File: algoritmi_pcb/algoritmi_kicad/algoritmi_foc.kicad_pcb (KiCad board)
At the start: 2 copper layers, 27 parts, among them IC1 MA710GQ-Z, IC2 AP2114HA-3.3TRG1, U1 TMC6300-LA-T

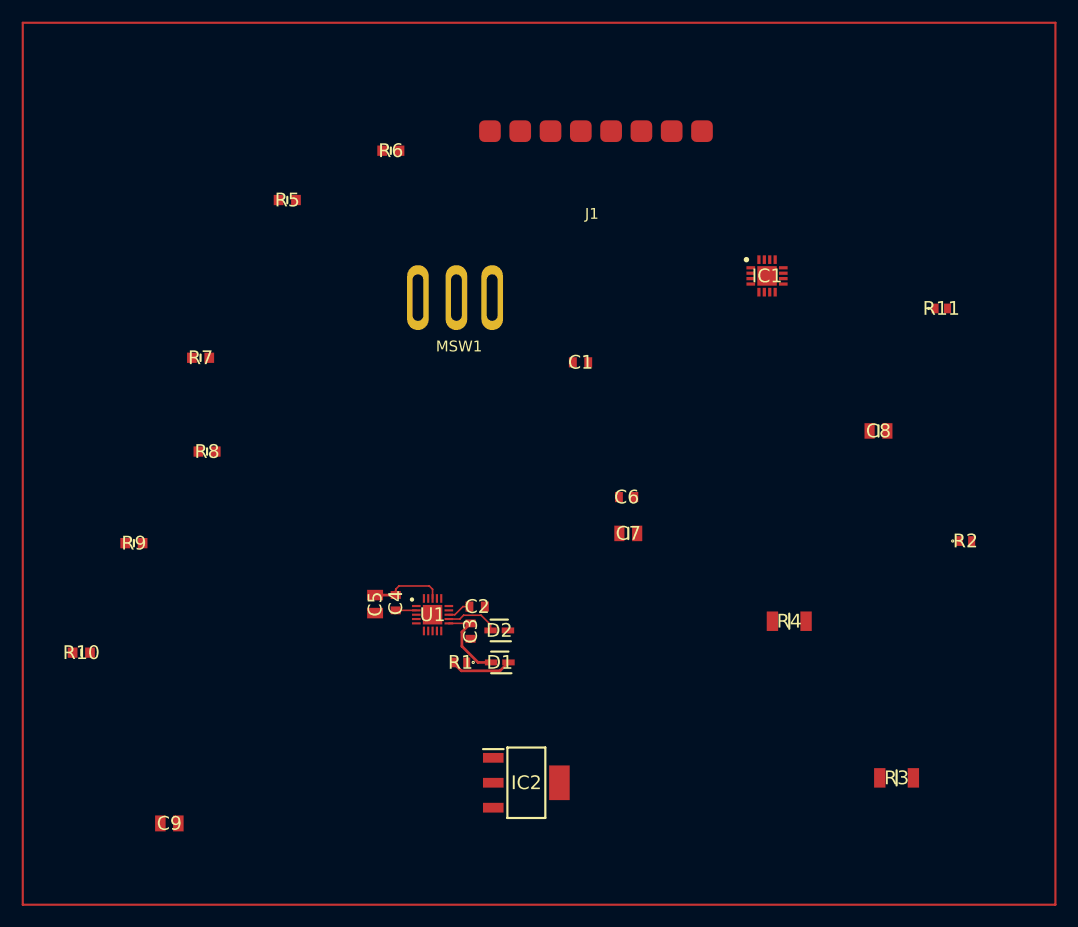
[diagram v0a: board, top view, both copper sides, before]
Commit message: Update PCB and Design
Design: added the connector for the motor.

PCB: added some constraints and essentially connected all the components to the TMC6300-LA-T.
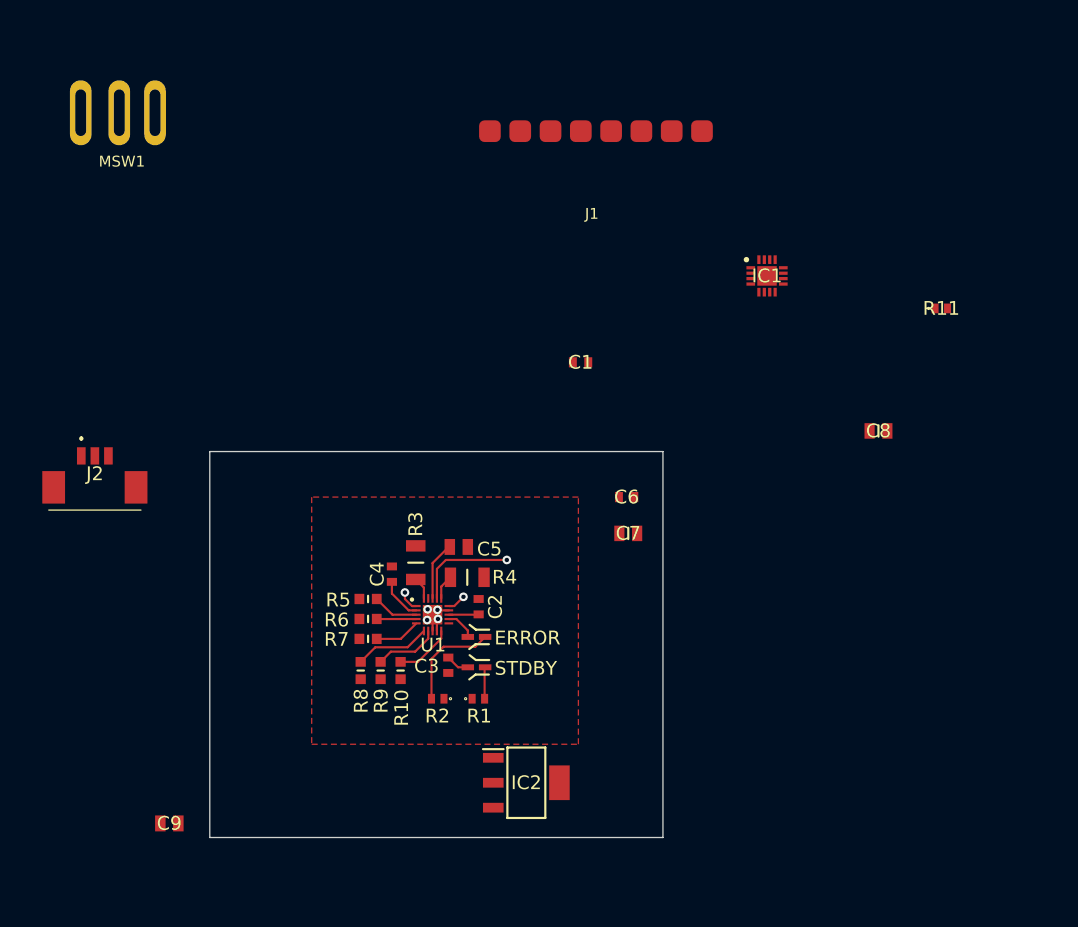
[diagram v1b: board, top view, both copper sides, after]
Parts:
- added J2: 53261-0371, SamacSys_Parts:532610371, F.Cu at (91.6, 106.3)
- moved R2 50.8 mm to (123.2, 125.8), turned to 180 degrees
- moved R3 48.6 mm to (121.2, 113.2), turned to 90 degrees
- moved R6 43.2 mm to (116.8, 118.4)
- moved R5 37.5 mm to (116.8, 116.6)
- moved MSW1 35.5 mm to (94.1, 76.8)
- moved R7 30.2 mm to (116.8, 120.3)
- moved R4 30.0 mm to (126.0, 114.6)
- moved R10 29.5 mm to (119.8, 123.2), turned to 90 degrees
- moved R9 25.6 mm to (118.0, 123.2), turned to 90 degrees
- moved R8 24.7 mm to (116.1, 123.2), turned to 90 degrees
- moved C5 9.35 mm to (125.2, 111.8), turned to 180 degrees
- moved C3 3.76 mm to (124.2, 122.7)
- moved R1 3.73 mm to (127.0, 125.8), turned to 0 degrees
- moved C4 2.65 mm to (119.0, 114.3)
- moved D1 2.20 mm to (126.8, 122.9)
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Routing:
- net V_OUT: track 0.00 -> 9.52 mm, vias 0 -> 1
- net Net-(D2-K): track 0.00 -> 9.47 mm
- net UL: track 0.00 -> 7.01 mm
- net GND: track 0.00 -> 6.24 mm, vias 0 -> 4
- net WL: track 0.00 -> 5.98 mm
- net Net-(D1-A): track 7.78 -> 2.17 mm
- net VL: track 0.00 -> 5.34 mm
- net UH: track 0.00 -> 4.25 mm
- net WH: track 0.00 -> 4.24 mm
- net VH: track 0.00 -> 3.65 mm
- net Net-(D1-K): track 5.72 -> 2.92 mm
- net BRUV: track 0.00 -> 2.30 mm
- net Net-(D2-A): track 4.88 -> 2.78 mm
- net VCP: track 1.90 -> 3.97 mm
- net BRW: track 0.00 -> 2.06 mm
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- added copper zone on F.Cu, net GND
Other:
- board outline added: 41.8 x 35.6 mm

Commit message: More PCB and Schematics Design
Also added components to the library.
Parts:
- added J3: SMM-115-02-S-D-LC-K-TR, SamacSys_Parts:SMM11502SDLCKTR, F.Cu at (179.0, 85.1)
- added MSW2: ~, solder_pads:solder_pads_4mm_3, F.Cu at (66.6, 133.5)
- added MSW3: ~, solder_pads:solder_pads_4mm_3, F.Cu at (66.6, 142.8)
- added MSW4: ~, solder_pads:solder_pads_4mm_3, F.Cu at (66.6, 152.0)
- added R12: 300R, SamacSys_Parts:ERJUP3, F.Cu at (73.5, 126.9)
- added R13: 300R, SamacSys_Parts:ERJUP3, F.Cu at (73.5, 130.8)
- added R14: 300R, SamacSys_Parts:ERJUP3, F.Cu at (73.5, 134.6)
- IC1: moved to B.Cu
- moved C5 144.3 mm to (269.4, 118.1)
- moved C3 144.3 mm to (268.4, 129.3)
- moved R3 144.3 mm to (265.4, 119.8)
- moved R4 144.3 mm to (270.1, 121.2)
- moved R9 144.3 mm to (262.1, 129.8)
- moved R1 144.3 mm to (271.1, 132.4)
- moved R2 144.3 mm to (267.4, 132.4)
- moved C2 144.3 mm to (271.1, 123.9)
- moved C4 144.3 mm to (263.1, 120.9)
- moved D1 144.3 mm to (270.9, 129.5)
- moved D2 144.3 mm to (270.9, 126.7)
- moved R10 144.3 mm to (263.9, 129.8)
- moved R5 144.3 mm to (260.9, 123.2)
- moved R6 144.3 mm to (260.9, 125.0)
- moved R7 144.3 mm to (260.9, 126.8)
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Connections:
- R11 pad 1: SW_OUT -> SW1_OUT
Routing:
- net VS: track 5.47 -> 20.2 mm
- net Net-(D2-K): track 9.47 -> 14.2 mm
- net Net-(D1-A): track 2.17 -> 5.80 mm
- net U_OUT: track 1.70 -> 4.00 mm, vias 1 -> 2
- net W_OUT: track 1.92 -> 4.13 mm, vias 1 -> 2
- net V_OUT: track 9.52 -> 10.1 mm, vias 1 -> 2
- removed copper zone on F.Cu, net GND

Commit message: PCB v0 Finished
PCB design ended, version 0
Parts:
- removed MSW1: ~, solder_pads:solder_pads_4mm_3
- removed R11: 300R, SamacSys_Parts:ERJUP3
- added H1: MotorHole, Holes:MountingHole_M1.6, F.Cu at (102.2, 66.6)
- added H2: MotorHole, Holes:MountingHole_M1.6, F.Cu at (86.9, 57.7)
- added H3: MotorHole, Holes:MountingHole_M1.6, F.Cu at (102.2, 48.8)
- added H4: MountHole, Holes:MountingHole_2.2mm_M2_ISO7380_Pad_NonVirtual, F.Cu at (97.1, 87.5)
- added H5: MountHole, Holes:MountingHole_2.2mm_M2_ISO7380_Pad_NonVirtual, F.Cu at (67.3, 57.7)
- added H6: MountHole, Holes:MountingHole_2.2mm_M2_ISO7380_Pad_NonVirtual, F.Cu at (97.1, 27.9)
- added H7: MountHole, Holes:MountingHole_2.2mm_M2_ISO7380_Pad_NonVirtual, F.Cu at (126.9, 57.7)
- C9, J1, J2: moved to B.Cu
- IC1: moved to F.Cu
- moved C3 146.5 mm to (127.1, 90.1)
- moved R3 146.5 mm to (124.1, 80.6)
- moved R9 146.5 mm to (120.9, 90.6)
- moved C5 146.5 mm to (128.2, 78.9)
- moved D1 146.5 mm to (129.7, 90.3)
- moved D2 146.5 mm to (129.7, 87.5)
- moved R1 146.5 mm to (129.9, 93.2)
- moved R10 146.5 mm to (122.7, 90.6)
- moved R2 146.5 mm to (126.2, 93.2)
- moved R5 146.5 mm to (119.7, 84.0)
- moved R6 146.5 mm to (119.7, 85.8)
- moved R7 146.5 mm to (119.7, 87.7)
- moved C2 146.5 mm to (129.9, 84.7)
- moved C4 146.5 mm to (121.9, 81.7)
- moved R8 146.5 mm to (119.1, 90.6)
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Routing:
- net VS: track 20.2 -> 256.7 mm, vias 0 -> 4
- net VL: track 5.34 -> 154.7 mm, vias 0 -> 2
- net WL: track 5.98 -> 154.2 mm, vias 0 -> 2
- net WH: track 4.24 -> 152.0 mm, vias 0 -> 2
- net UL: track 7.01 -> 151.6 mm, vias 0 -> 2
- net VH: track 3.65 -> 147.3 mm, vias 0 -> 2
- net UH: track 4.25 -> 124.3 mm, vias 0 -> 2
- net +3.3V: track 0.00 -> 101.1 mm, vias 0 -> 1
- net GND: track 6.24 -> 106.1 mm, vias 4 -> 22
- net PWM_OUT: track 0.00 -> 77.2 mm, vias 0 -> 4
- net CS_MAG: track 0.00 -> 70.5 mm
- net SW2_OUT: track 0.00 -> 68.8 mm, vias 0 -> 2
- net MISO_MAG: track 0.00 -> 66.8 mm, vias 0 -> 4
- net CLK_MAG: track 0.00 -> 52.9 mm
- net B_OUT: track 0.00 -> 48.7 mm, vias 0 -> 2
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- added copper zone on B.Cu, net GND
- added copper zone on F.Cu, net GND
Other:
- board size 41.8 x 35.6 mm -> 81.2 x 81.2 mm
- board text added: "5V 5V GND GND M_CS M_CLK M_MISO M_MOSI A B Z PWM SW4 SW3"
- board text added: "Algoritmi FOC SmartKnob"
- board text added: "Base PCB 1.0"
- board text added: "LCD"
- board text added: "MGH"
- board text added: "MGL"
- board text added: "MOTOR"
- board text added: "UH VH WH UL VL WL SW1 SW2 L_DI L_CLK L_CS L_DC L_RST L_BL"

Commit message: changes
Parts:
- removed C6: 1uF, SamacSys_Parts:CAPC1608X90N
- removed H1, H2, H3: MotorHole, Holes:MountingHole_M1.6
- removed H4, H5, H6, H7: MountHole, Holes:MountingHole_2.2mm_M2_ISO7380_Pad_NonVirtual
- removed IC1: MA710GQ-Z, SamacSys_Parts:QFN50P300X300X100-17N-D
- removed MSW2, MSW3, MSW4: ~, solder_pads:solder_pads_4mm_3
- removed R12, R13, R14: 300R, SamacSys_Parts:ERJUP3
- C1, C2, C3, C4: footprint SamacSys_Parts:CAPC1608X90N -> Capacitor_SMD:C_0201_0603Metric
- C5: footprint SamacSys_Parts:CAPC2012X145N -> Capacitor_SMD:C_0805_2012Metric
- C7, C8: footprint SamacSys_Parts:CAPC2012X140N -> Capacitor_SMD:C_0805_2012Metric
- C9: footprint SamacSys_Parts:CAPC2012X145N -> Capacitor_SMD:C_0805_2012Metric; moved to F.Cu
- D1, D2: footprint SamacSys_Parts:LEDM1620X150N -> LED_SMD:LED_0603_1608Metric
- IC2: footprint SamacSys_Parts:SOT230P700X180-4N -> Package_TO_SOT_SMD:SOT-223-3_TabPin2
- J1, J2: moved to F.Cu
- J3: value SMM-115-02-S-D-LC-K-TR -> SMM-110-02-H-D-K-TR; footprint SamacSys_Parts:SMM11502SDLCKTR -> SamacSys_Parts:SMM-110-02-XX-D-K-TR
- R1, R2: value 300R -> 300; footprint SamacSys_Parts:ERJUP3 -> Resistor_SMD:R_0201_0603Metric
- R10, R5, R6, R7, R8, R9: footprint SamacSys_Parts:RESC1608X55N -> Resistor_SMD:R_0201_0603Metric
- R3, R4: footprint SamacSys_Parts:RESC3216X70N -> Resistor_SMD:R_1206_3216Metric
- moved J2 81.4 mm to (31.2, 67.8), turned to -90 degrees
- moved C8 73.3 mm to (60.9, 62.8), turned to 0 degrees
- moved C5 70.8 mm to (60.9, 56.8), turned to 0 degrees
- moved IC2 60.1 mm to (52.4, 117.2)
- moved J3 56.6 mm to (44.7, 89.4)
- moved C7 52.3 mm to (60.9, 59.8), turned to 0 degrees
- moved R1 46.6 mm to (83.6, 88.4)
- moved D1 44.6 mm to (85.2, 87.2), turned to 90 degrees
- moved C3 43.7 mm to (83.6, 86.4), turned to 0 degrees
- moved D2 42.7 mm to (87.0, 87.2), turned to 90 degrees
- moved C2 41.3 mm to (88.7, 86.2), turned to 180 degrees
- moved R2 37.9 mm to (88.6, 88.4), turned to 0 degrees
- moved R4 37.5 mm to (91.8, 85.2), turned to -90 degrees
- moved U1 37.4 mm to (88.4, 82.0), turned to -90 degrees
- moved R7 34.4 mm to (86.6, 78.6), turned to -90 degrees
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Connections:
- J2 pad 1: U_OUT -> W_OUT
- J2 pad 3: W_OUT -> U_OUT
- J3 pad 1: LCD_BL -> E_DO
- J3 pad 10: B_OUT -> LCD_RESET
- J3 pad 11: LCD_DATA_IN -> VL
- J3 pad 12: A_OUT -> LCD_BL
- J3 pad 13: unconnected-(J3-Pad13) -> UL
- J3 pad 14: unconnected-(J3-Pad14) -> GND
- J3 pad 15: SW2_OUT -> WH
- J3 pad 16: MOSI_MAG -> GND
- J3 pad 17: SW1_OUT -> VH
- J3 pad 18: MISO_MAG -> VS
- J3 pad 19: WL -> UH
- J3 pad 2: SW4_OUT -> LCD_DATA_IN
- J3 pad 20: CLK_MAG -> VS
- J3 pad 3: LCD_RESET -> E_CLK
- J3 pad 4: SW3_OUT -> LCD_CLOCK
- J3 pad 5: LCD_DC -> E_CSN
- J3 pad 6: PWM_OUT -> LCD_CS
- J3 pad 7: LCD_CS -> GND
- J3 pad 8: Z_OUT -> LCD_DC
- J3 pad 9: LCD_CLOCK -> WL
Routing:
- net VS: track 256.7 -> 3.07 mm, vias 4 -> 0
- net VL: track 154.7 -> 0.00 mm, vias 2 -> 0
- net WL: track 154.2 -> 0.00 mm, vias 2 -> 0
- net UL: track 151.6 -> 0.00 mm, vias 2 -> 0
- net WH: track 152.0 -> 1.99 mm, vias 2 -> 0
- net VH: track 147.3 -> 1.83 mm, vias 2 -> 0
- net UH: track 124.3 -> 1.66 mm, vias 2 -> 0
- net GND: track 106.1 -> 0.00 mm, vias 22 -> 0
- net +3.3V: track 101.1 -> 0.00 mm, vias 1 -> 0
- net PWM_OUT: track 77.2 -> 0.00 mm, vias 4 -> 0
- net CS_MAG: track 70.5 -> 0.00 mm
- net SW2_OUT: track 68.8 -> 0.00 mm, vias 2 -> 0
- net MISO_MAG: track 66.8 -> 0.00 mm, vias 4 -> 0
- net CLK_MAG: track 52.9 -> 0.00 mm
- net B_OUT: track 48.7 -> 0.00 mm, vias 2 -> 0
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- removed copper zone on B.Cu, net GND
- removed copper zone on F.Cu, net GND
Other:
- board outline removed
- board text removed: "5V 5V GND GND M_CS M_CLK M_MISO M_MOSI A B Z PWM SW4 SW3"
- board text removed: "Algoritmi FOC SmartKnob"
- board text removed: "Base PCB 1.0"
- board text removed: "LCD"
- board text removed: "MGH"
- board text removed: "MGL"
- board text removed: "MOTOR"
- board text removed: "UH VH WH UL VL WL SW1 SW2 L_DI L_CLK L_CS L_DC L_RST L_BL"

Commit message: updates
updates to the pcb
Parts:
- moved R8 52.6 mm to (85.4, 80.8)
- moved R9 52.5 mm to (85.4, 81.8)
- moved R10 52.4 mm to (85.4, 83.4)
- moved C1 20.2 mm to (89.0, 76.0), turned to -90 degrees
- moved R2 1.40 mm to (88.7, 87.0)
- moved R1 0.45 mm to (83.8, 88.0), turned to 90 degrees
- moved C3 0.20 mm to (83.8, 86.4), turned to -90 degrees
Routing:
- net Net-(D2-K): track 0.00 -> 2.52 mm
- net VS: track 3.07 -> 5.03 mm
- net Net-(D1-K): track 0.00 -> 1.53 mm
- net VL: track 0.00 -> 1.43 mm
- net UL: track 0.00 -> 1.35 mm
- net WL: track 0.00 -> 1.26 mm

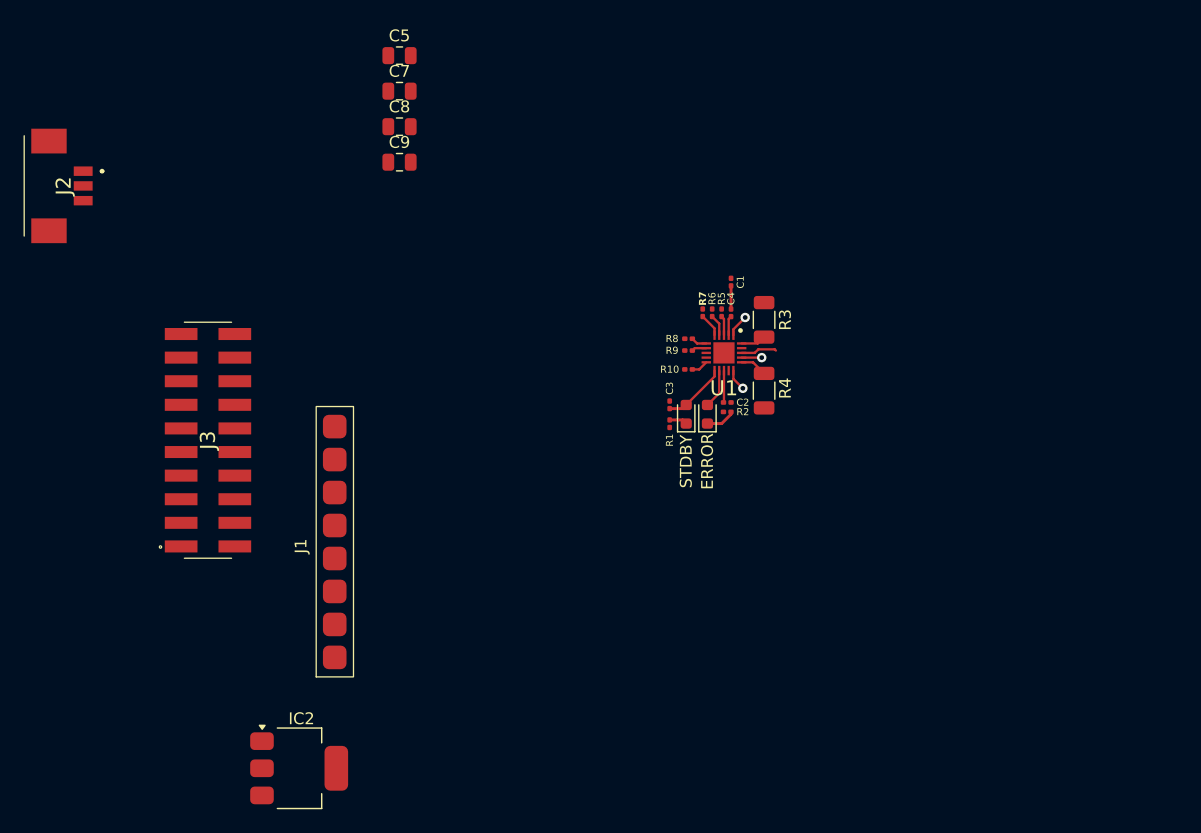
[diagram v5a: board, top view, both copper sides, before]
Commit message: finished base pcb
in the last meeting with professor, we decided to separate the smartknob into 3 pcb's, one that contains the encoder and the motor, the other that contains the connectors and motor driver, and another one that contains the lcd
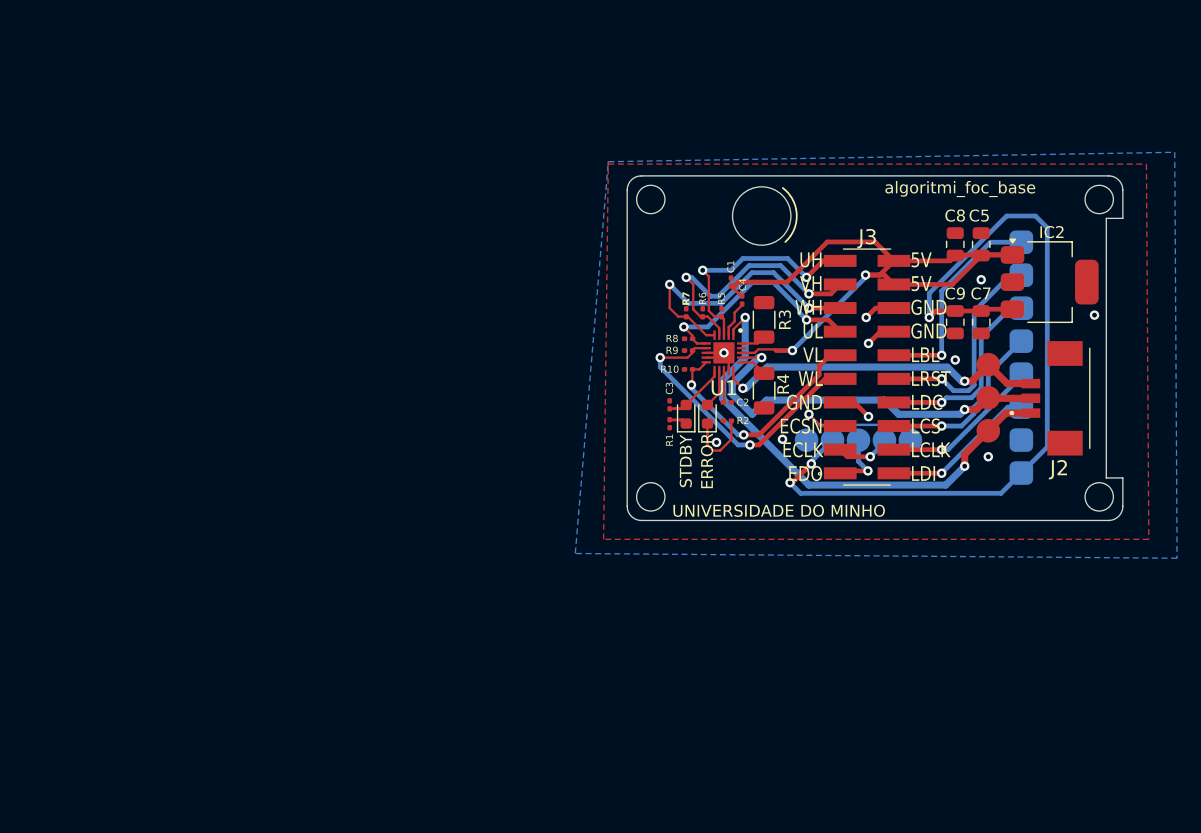
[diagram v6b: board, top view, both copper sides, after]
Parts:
- added REF**: SolderWirePad_1x01_SMD_1x2mm, Connector_Wire:SolderWirePad_1x01_SMD_1x2mm, F.Cu at (110.8, 83.0)
- added REF**: SolderWirePad_1x01_SMD_1x2mm, Connector_Wire:SolderWirePad_1x01_SMD_1x2mm, F.Cu at (110.8, 88.6)
- added REF**: SolderWirePad_1x01_SMD_1x2mm, Connector_Wire:SolderWirePad_1x01_SMD_1x2mm, F.Cu at (110.8, 85.8)
- added REF**: SolderWirePad_1x01_SMD_1x2mm, Connector_Wire:SolderWirePad_1x01_SMD_1x2mm, B.Cu at (97.6, 89.4)
- added REF**: SolderWirePad_1x01_SMD_1x2mm, Connector_Wire:SolderWirePad_1x01_SMD_1x2mm, B.Cu at (104.2, 89.4)
- added REF**: SolderWirePad_1x01_SMD_1x2mm, Connector_Wire:SolderWirePad_1x01_SMD_1x2mm, B.Cu at (95.4, 89.4)
- added REF**: SolderWirePad_1x01_SMD_1x2mm, Connector_Wire:SolderWirePad_1x01_SMD_1x2mm, B.Cu at (99.8, 89.4)
- added REF**: SolderWirePad_1x01_SMD_1x2mm, Connector_Wire:SolderWirePad_1x01_SMD_1x2mm, B.Cu at (102.0, 89.4)
- J1: moved to B.Cu
- moved J2 88.0 mm to (117.3, 85.8), turned to 90 degrees
- moved IC2 75.8 mm to (116.0, 76.0)
- moved J3 56.2 mm to (100.5, 83.2)
- moved J1 55.4 mm to (111.1, 82.8)
- moved C7 53.0 mm to (110.2, 79.4), turned to 90 degrees
- moved C5 51.8 mm to (110.2, 72.8), turned to -90 degrees
- moved C9 49.0 mm to (108.0, 79.4), turned to 90 degrees
- moved C8 48.1 mm to (108.0, 72.8), turned to -90 degrees
- moved C4 1.44 mm to (89.9, 77.5)
- moved R7 1.40 mm to (85.2, 78.6)
- moved R6 0.80 mm to (86.6, 78.6)
- moved R2 0.75 mm to (88.7, 87.8)
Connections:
- IC2 pad 2: unconnected-(IC2-GND_1-Pad2)_1 -> GND
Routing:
- net +3.3V: track 0.00 -> 70.1 mm, vias 0 -> 3
- net VS: track 5.03 -> 57.7 mm, vias 0 -> 2
- net W_OUT: track 1.91 -> 41.8 mm, vias 1 -> 2
- net V_OUT: track 1.70 -> 33.6 mm, vias 1 -> 2
- net U_OUT: track 1.83 -> 28.7 mm, vias 1 -> 2
- net WL: track 1.26 -> 25.5 mm, vias 0 -> 2
- net WH: track 1.99 -> 24.2 mm, vias 0 -> 2
- net VH: track 1.83 -> 22.5 mm, vias 0 -> 2
- net VL: track 1.43 -> 20.5 mm, vias 0 -> 2
- net LCD_RESET: track 0.00 -> 18.9 mm, vias 0 -> 1
- net UH: track 1.66 -> 19.9 mm, vias 0 -> 2
- net UL: track 1.35 -> 19.4 mm, vias 0 -> 2
- net LCD_BL: track 0.00 -> 18.0 mm, vias 0 -> 1
- net LCD_DC: track 0.00 -> 16.6 mm, vias 0 -> 1
- net LCD_CS: track 0.00 -> 15.0 mm, vias 0 -> 1
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- added copper zone on B.Cu, net GND
- added copper zone on F.Cu, net GND
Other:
- board outline added: 42 x 29.2 mm
- board text added: "5V 5V GND GND LBL LRST LDC LCS LCLK LDI"
- board text added: "BL RST DC CS CLK DI GND 3.3V"
- board text added: "ENC"
- board text added: "GND 3.3V DO CLK CSN"
- board text added: "SMARTKNOB"
- board text added: "UH VH WH UL VL WL GND ECSN ECLK EDO"
- board text added: "UNIVERSIDADE DO MINHO"
- board text added: "algoritmi_foc_base"

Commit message: some changes to schematics
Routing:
- removed copper zone on B.Cu, net GND
- removed copper zone on F.Cu, net GND
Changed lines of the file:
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@@
 		(tags "capacitor")
 		(property "Reference" "C5"
-			(at -2.4 0.15 360)
+			(at -2.4 0.15 0)
 			(layer "F.SilkS")
 			(effects
@@
 		(tags "Connector")
 		(property "Reference" "J3"
-			(at -11 -0.075 360)
+			(at -11 -0.075 0)
 			(layer "F.SilkS")
 			(effects
@@
 		(tags "capacitor")
 		(property "Reference" "C8"
-			(at -2.4 0 360)
+			(at -2.4 0 0)
 			(layer "F.SilkS")
 			(effects
@@
 	)
 	(zone
-		(net 1)
-		(net_name "GND")
-		(layer "F.Cu")
-		(hatch edge 0.5)
-		(connect_pads
-			(clearance 0)
-		)
-		(min_thickness 0.25)
-		(filled_areas_thickness no)
-		(fill yes
-			(thermal_gap 0.5)
-			(thermal_bridge_width 0.5)
-		)
-		(polygon
-			(pts
-				(xy 78.6 66) (xy 124.2 66) (xy 124.4 97.8) (xy 78.2 97.8) (xy 78.6 65.8)
-			)
-		)
-	)
-	(zone
 		(net 0)
 		(net_name "")
@@
 			)
 		)
-	)
-	(zone
-		(net 1)
-		(net_name "GND")
-		(layer "B.Cu")
-		(hatch edge 0.5)
-		(priority 1)
-		(connect_pads
-			(clearance 0)
-		)
-		(min_thickness 0.25)
-		(filled_areas_thickness no)
-		(fill yes
-			(thermal_gap 0.5)
-			(thermal_bridge_width 0.5)
-		)
-		(polygon
-			(pts
-				(xy 78.6 65.8) (xy 126.6 65) (xy 126.8 99.4) (xy 75.8 99)
-			)
-		)
